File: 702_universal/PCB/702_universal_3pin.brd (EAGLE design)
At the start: 25.4 x 33 mm, 12 parts

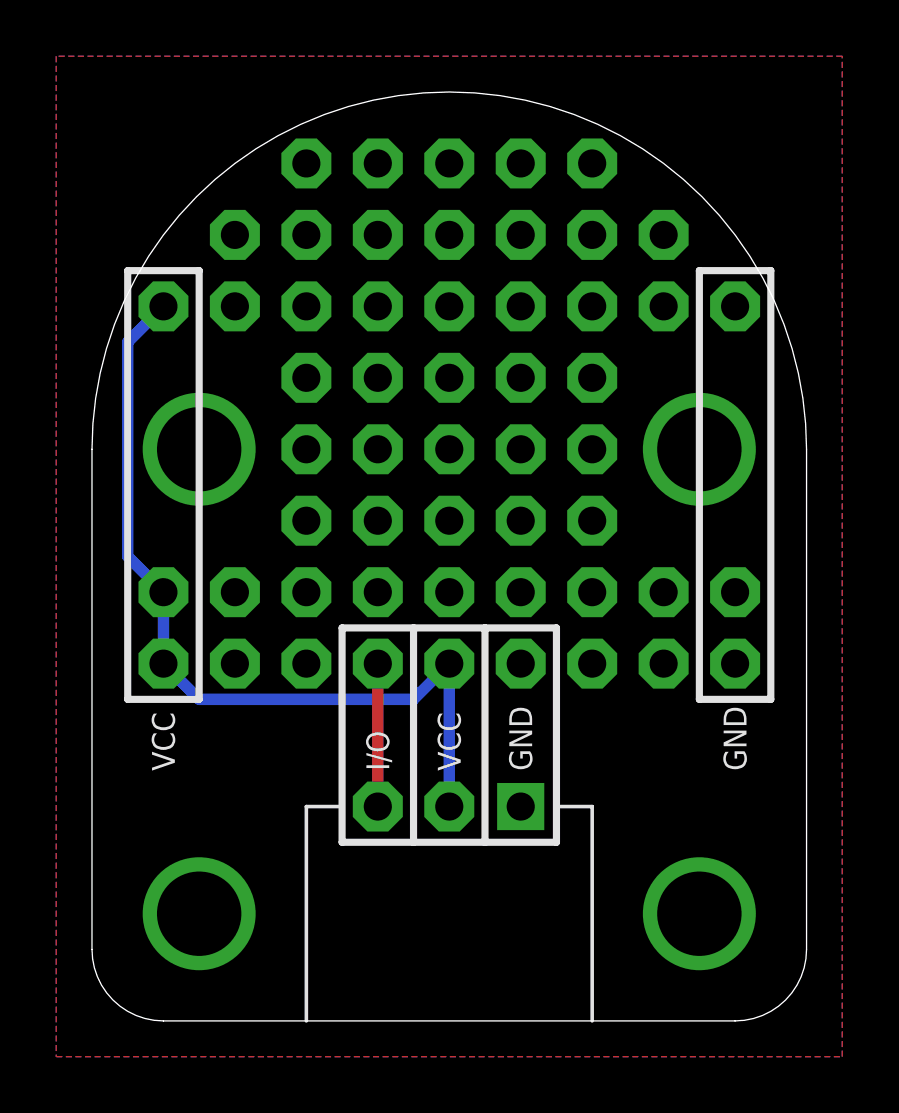
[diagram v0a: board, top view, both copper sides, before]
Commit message: add product number
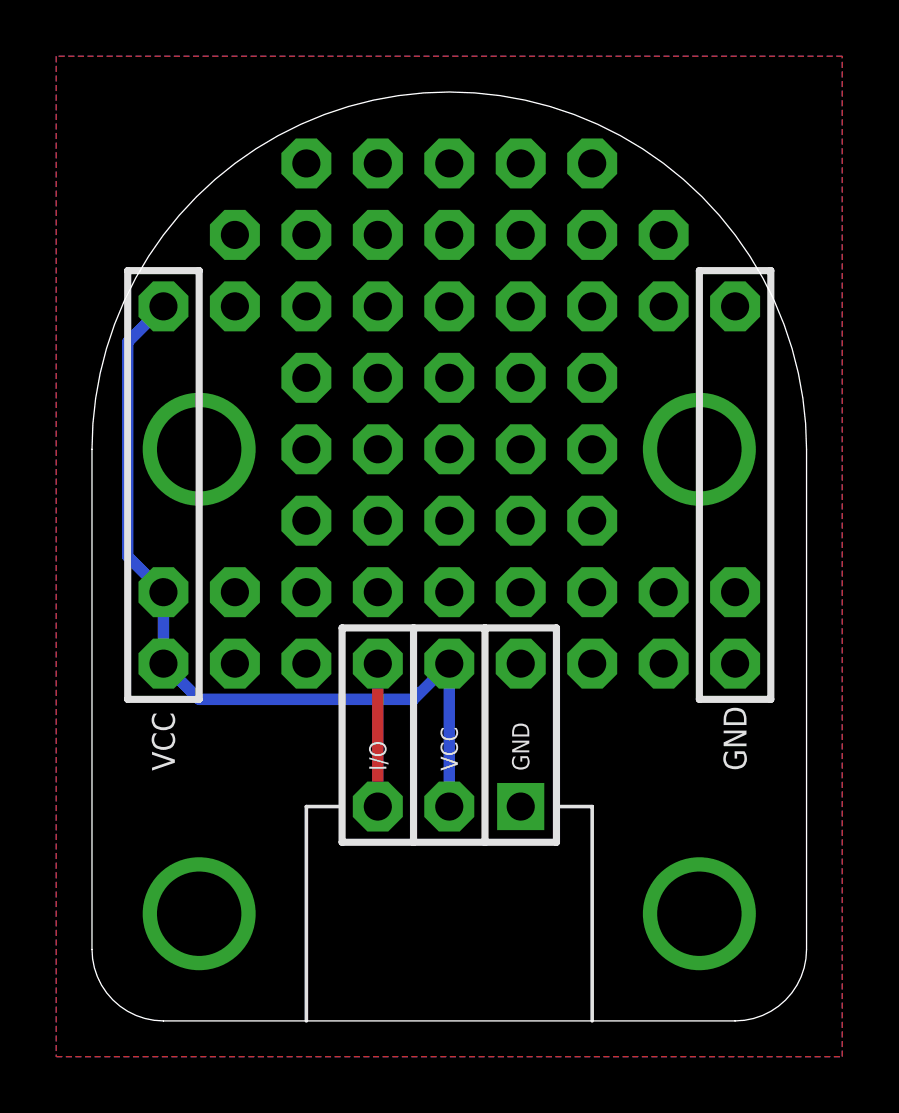
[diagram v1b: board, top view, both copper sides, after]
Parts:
- U$3: device FaBo-etc:LOGO_FABO_M_BOTTOM -> FaBo-etc:LOGO_FABO_MS_BOTTOM
- moved U$1 17.8 mm to (3.81, 8.89)
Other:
- board text added: "#702"
- board text added: "Rev.1.0.1"
- board text removed: "Rev.1.0.0"
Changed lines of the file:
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@@
 <setting verticaltext="up"/>
 </settings>
-<grid distance="0.05" unitdist="inch" unit="inch" style="lines" multiple="1" display="yes" altdistance="0.025" altunitdist="inch" altunit="inch"/>
+<grid distance="0.025" unitdist="inch" unit="inch" style="lines" multiple="1" display="yes" altdistance="0.025" altunitdist="inch" altunit="inch"/>
 <layers>
 <layer number="1" name="Top" color="4" fill="1" visible="yes" active="yes"/>
@@
 <text x="22.86" y="8.89" size="0.8128" layer="21" font="vector" ratio="12" rot="R90" align="center-left">GND</text>
 <text x="2.54" y="8.89" size="0.8128" layer="21" font="vector" ratio="12" rot="R90" align="center-left">VCC</text>
-<text x="12.7" y="1.27" size="1.016" layer="22" font="vector" ratio="12" rot="MR0" align="bottom-center">MADE IN JAPAN</text>
-<text x="1.27" y="5.715" size="0.8128" layer="22" font="vector" ratio="12" rot="MR90">Rev.1.0.0</text>
+<text x="12.7" y="2.54" size="0.8128" layer="22" font="vector" ratio="12" rot="MR180" align="bottom-center">MADE IN JAPAN</text>
+<text x="12.7" y="9.525" size="1.016" layer="22" font="vector" ratio="12" rot="MR0" align="bottom-center">Rev.1.0.1</text>
+<text x="21.59" y="8.255" size="1.778" layer="22" font="vector" ratio="12" rot="MR0" align="bottom-center">#702</text>
 </plain>
 <attributes>
@@
 <element name="J9" library="FaBo-etc" package="PIN_1X1_NONAME" value="" x="22.86" y="15.24"/>
 <element name="J10" library="FaBo-etc" package="PIN_1X1_NONAME" value="" x="22.86" y="25.4"/>
-<element name="U$1" library="FaBo-etc" package="LOGO_OSHW_S_BOTTOM" value="" x="21.59" y="8.89"/>
-<element name="U$3" library="FaBo-etc" package="LOGO_FABO_M_BOTTOM" value="" x="12.7" y="2.54"/>
+<element name="U$1" library="FaBo-etc" package="LOGO_OSHW_S_BOTTOM" value="" x="3.81" y="8.89"/>
+<element name="U$3" library="FaBo-etc" package="LOGO_FABO_MS_BOTTOM" value="" x="12.7" y="2.54"/>
 </elements>
 <signals>
